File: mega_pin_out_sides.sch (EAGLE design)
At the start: 31 parts, among them T1 2N2222, T2 2N2222, T3 2N2222, T4 2N2222

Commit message: Continue side Schematic design and layout
Almost finished first trail for board layout.
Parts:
- added OK10, OK11, OK12, OK13, OK14, OK15, OK16, OK17, OK18, OK5, OK6, OK7, OK8, OK9: PC817, optocoupler:PC817
- added R10, R11, R12, R13, R14, R15, R16, R17, R18, R19, R20, R21, R22, R23, R24, R25, R26, R27, R28, R29, R30, R31, R32, R33, R34, R35, R36, R9: (no value), resistor:R-US_M1206
- added T10, T11, T12, T13, T14, T15, T16, T17, T18, T5, T6, T7, T8, T9: 2N2222, transistor:2N2222
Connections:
- removed net N$16: X1-5.KL
- new net 0: PWML.1, R23.1
- new net 0BJT: T12.C, X2-2.KL
- new net 14: COMMUNICATION.8, R25.1
- new net 14BJT: T13.C, X2-3.KL
- new net 15: COMMUNICATION.7, R27.1
- new net 15BJT: T14.C, X2-4.KL
- new net 16: COMMUNICATION.6, R29.1
- new net 16BJT: T15.C, X2-5.KL
- new net 17: COMMUNICATION.5, R31.1
- new net 17BJT: T16.C, X2-6.KL
- new net 18: COMMUNICATION.4, R33.1
- new net 18BJT: T17.C, X2-7.KL
- new net 19: COMMUNICATION.3, R35.1
- new net 19BJT: T18.C, X2-8.KL
- new net 2: PWML.3, R21.1
- new net 2BJT: T11.C, X2-1.KL
- new net 3: PWML.4, R19.1
- new net 3BJT: T10.C, X1-10.KL
- new net 4: PWML.5, R17.1
- new net 4BJT: T9.C, X1-9.KL
- new net 5: PWML.6, R15.1
- new net 5BJT: T8.C, X1-8.KL
- new net 6: PWML.7, R13.1
- new net 6BJT: T7.C, X1-7.KL
- new net 7: PWML.8, R11.1
- new net 7BJT: T6.C, X1-6.KL
- new net 8: JP6.10, R9.1
- new net 8BJT: T5.C, X1-5.KL
- new net N$14: OK5.A, R9.2
- new net N$15: OK5.EMIT, R10.1
- new net N$22: R10.2, T5.B
- new net N$23: OK6.A, R11.2
- new net N$24: OK6.EMIT, R12.1
- new net N$25: R12.2, T6.B
- new net N$26: OK7.A, R13.2
- new net N$27: OK7.EMIT, R14.1
- new net N$28: R14.2, T7.B
- new net N$29: OK8.A, R15.2
- new net N$30: OK8.EMIT, R16.1
- new net N$31: R16.2, T8.B
- new net N$32: OK9.A, R17.2
- new net N$33: OK9.EMIT, R18.1
- new net N$34: R18.2, T9.B
- new net N$35: OK10.A, R19.2
- new net N$36: OK10.EMIT, R20.1
- new net N$37: R20.2, T10.B
- new net N$38: OK11.A, R21.2
- new net N$39: OK11.EMIT, R22.1
- new net N$40: R22.2, T11.B
- new net N$41: OK16.A, R31.2
- new net N$42: OK16.EMIT, R32.1
- new net N$43: R32.2, T16.B
- new net N$44: OK12.A, R23.2
- new net N$45: OK12.EMIT, R24.1
- new net N$46: R24.2, T12.B
- new net N$47: OK13.A, R25.2
- new net N$48: OK13.EMIT, R26.1
- new net N$49: R26.2, T13.B
- new net N$50: OK14.A, R27.2
- new net N$51: OK14.EMIT, R28.1
- new net N$52: R28.2, T14.B
- new net N$53: OK15.A, R29.2
- new net N$54: OK15.EMIT, R30.1
- new net N$55: R30.2, T15.B
- new net N$56: OK18.A, R35.2
- new net N$57: OK18.EMIT, R36.1
- new net N$58: R36.2, T18.B
- new net N$59: OK17.A, R33.2
- new net N$60: OK17.EMIT, R34.1
- new net N$61: R34.2, T17.B
- new net N$77: COMMUNICATION.2
- new net N$78: COMMUNICATION.1
- new net N$92: X2-9.KL
- new net N$93: X2-10.KL
- net GND: now also OK10.C, OK11.C, OK12.C, OK13.C, OK14.C, OK15.C, OK16.C, OK17.C, OK18.C, OK5.C, OK6.C, OK7.C, OK8.C, OK9.C, T10.E, T11.E, T12.E, T13.E, T14.E, T15.E, T16.E, T17.E, T18.E, T5.E, T6.E, T7.E, T8.E, T9.E
- net VEXT: now also OK10.COL, OK11.COL, OK12.COL, OK13.COL, OK14.COL, OK15.COL, OK16.COL, OK17.COL, OK18.COL, OK5.COL, OK6.COL, OK7.COL, OK8.COL, OK9.COL
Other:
- moved on the sheet: C1, C2, OK1, OK2, OK3, OK4, R1, R2, R3, R4, R5, R6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

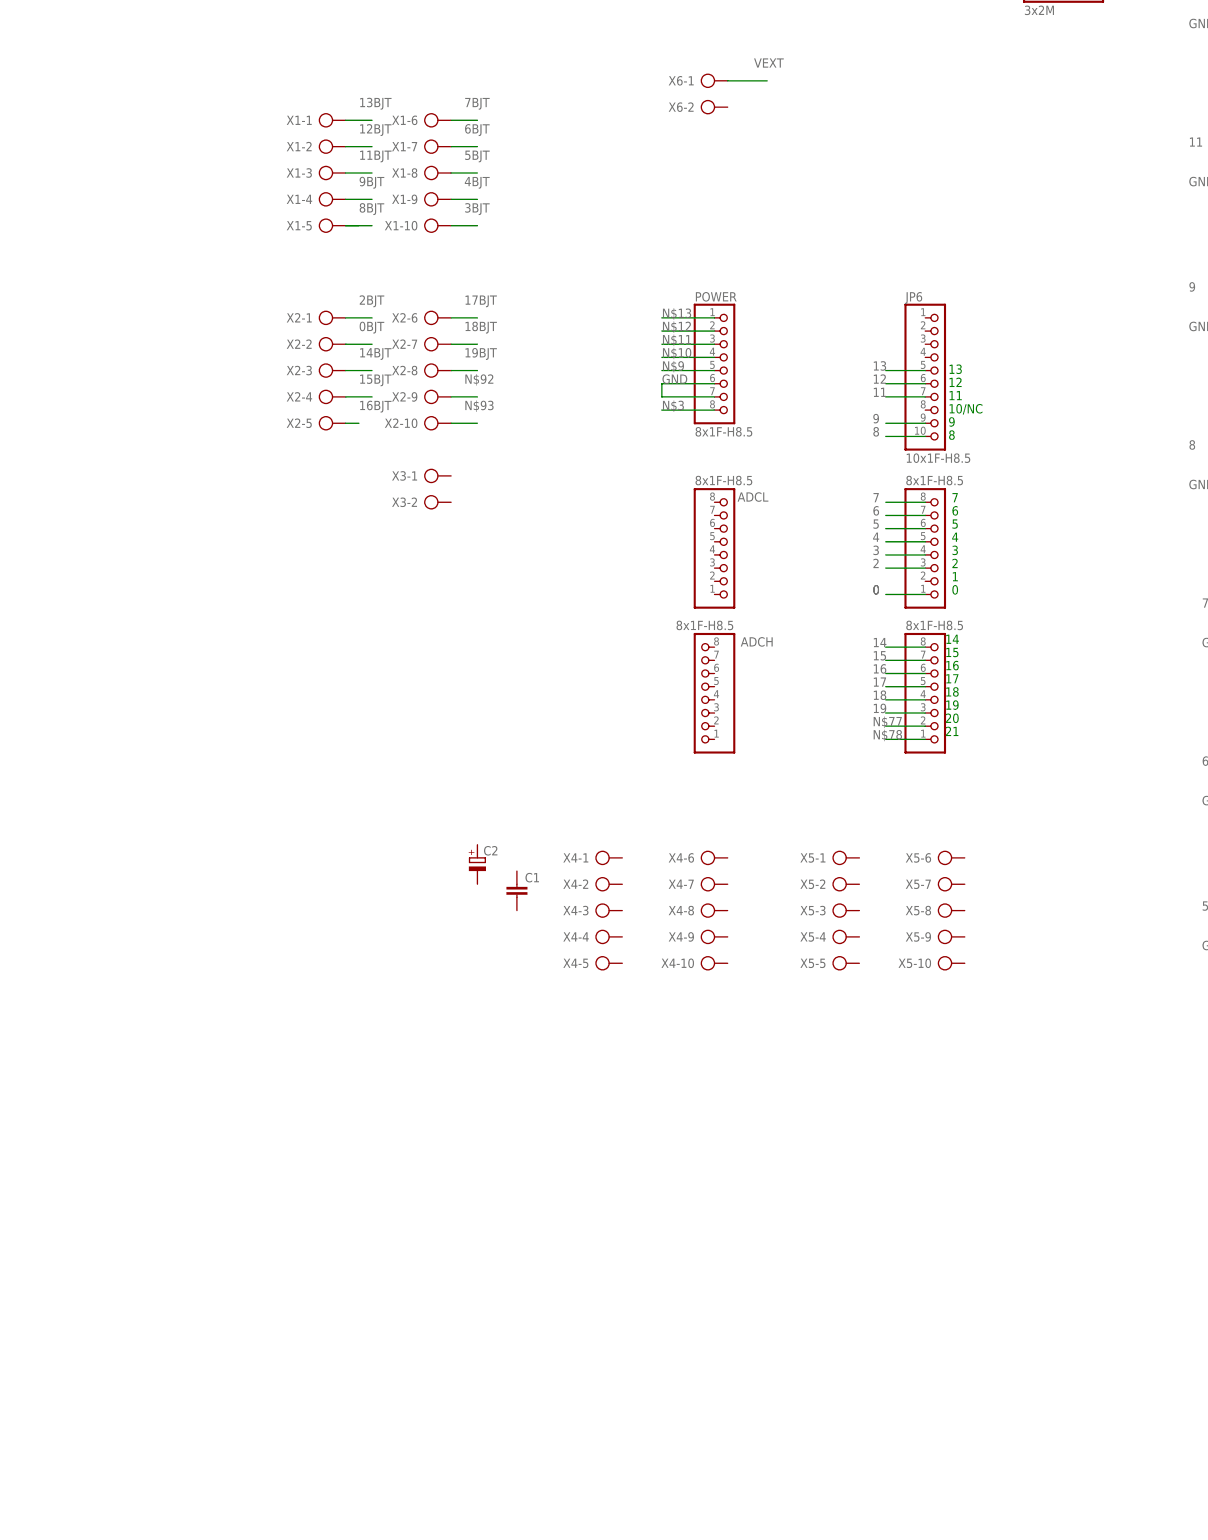
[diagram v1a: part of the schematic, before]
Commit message: [SIDES] New design proposal
- In this commit the layout was completely changed. Opto are grouped in the center while BJT was beside the terminal blocks.

TODO: complete the Analogue side.
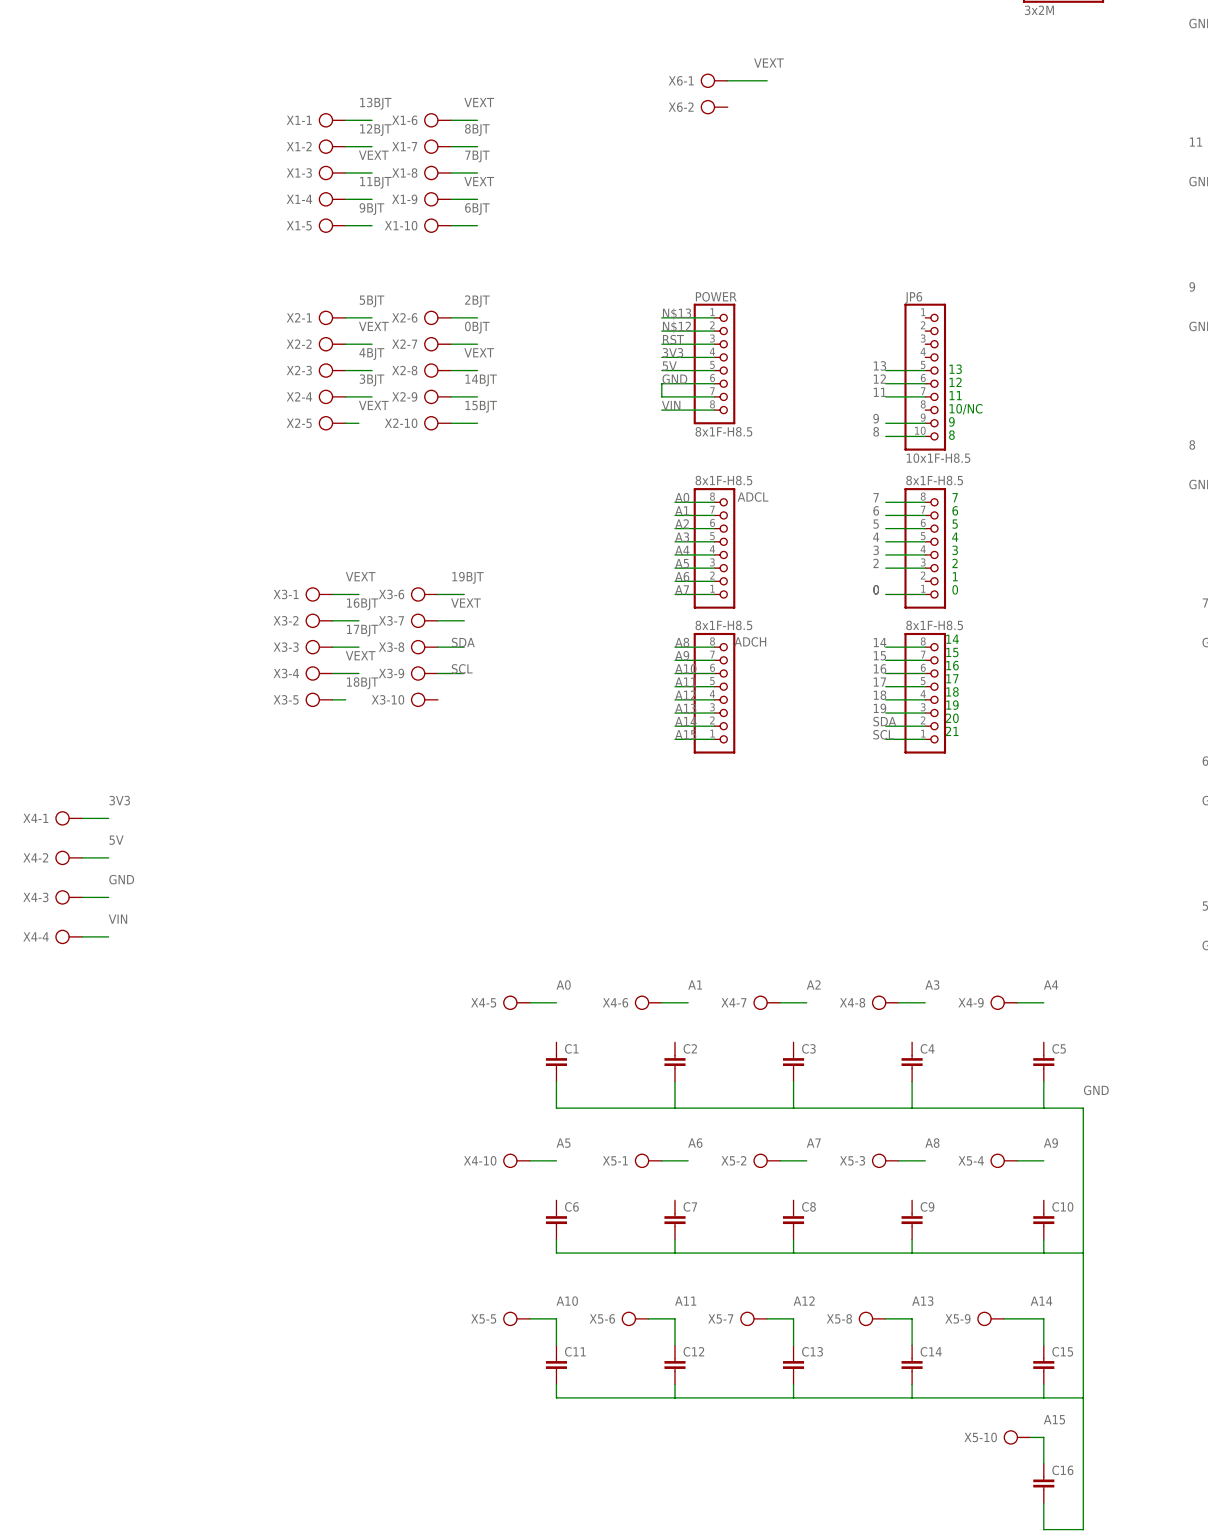
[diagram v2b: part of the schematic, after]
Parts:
- added C10, C11, C12, C13, C14, C15, C16, C3, C4, C5, C6, C7, C8, C9: (no value), resistor:C-EUC1206
- C2: device rcl:CPOL-EUE2.5-6 -> resistor:C-EUC1206
- X3: device con-ptr500:AK500/2 -> con-ptr500:AK500/10
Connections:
- net N$11 renamed RST
- removed net N$10: POWER.4
- removed net N$3: POWER.8
- removed net N$77: COMMUNICATION.2
- removed net N$78: COMMUNICATION.1
- removed net N$9: POWER.5
- removed net N$92: X2-9.KL
- removed net N$93: X2-10.KL
- new net 3V3: POWER.4, X4-1.KL
- new net 5V: POWER.5, X4-2.KL
- new net A0: ADCL.8, X4-5.KL
- new net A1: ADCL.7, X4-6.KL
- new net A10: ADCH.6, C11.1, X5-5.KL
- new net A11: ADCH.5, C12.1, X5-6.KL
- new net A12: ADCH.4, C13.1, X5-7.KL
- new net A13: ADCH.3, C14.1, X5-8.KL
- new net A14: ADCH.2, C15.1, X5-9.KL
- new net A15: ADCH.1, C16.1, X5-10.KL
- new net A2: ADCL.6, X4-7.KL
- new net A3: ADCL.5, X4-8.KL
- new net A4: ADCL.4, X4-9.KL
- new net A5: ADCL.3, X4-10.KL
- new net A6: ADCL.2, X5-1.KL
- new net A7: ADCL.1, X5-2.KL
- new net A8: ADCH.8, X5-3.KL
- new net A9: ADCH.7, X5-4.KL
- new net SCL: COMMUNICATION.1, X3-9.KL
- new net SDA: COMMUNICATION.2, X3-8.KL
- new net VIN: POWER.8, X4-4.KL
- net 0BJT: now also X2-7.KL; no longer X2-2.KL
- net 11BJT: now also X1-4.KL; no longer X1-3.KL
- net 14BJT: now also X2-9.KL; no longer X2-3.KL
- net 15BJT: now also X2-10.KL; no longer X2-4.KL
- net 16BJT: now also X3-2.KL; no longer X2-5.KL
- net 17BJT: now also X3-3.KL; no longer X2-6.KL
- net 18BJT: now also X3-5.KL; no longer X2-7.KL
- net 19BJT: now also X3-6.KL; no longer X2-8.KL
- net 2BJT: now also X2-6.KL; no longer X2-1.KL
- net 3BJT: now also X2-4.KL; no longer X1-10.KL
- net 4BJT: now also X2-3.KL; no longer X1-9.KL
- net 5BJT: now also X2-1.KL; no longer X1-8.KL
- net 6BJT: now also X1-10.KL; no longer X1-7.KL
- net 7BJT: now also X1-8.KL; no longer X1-6.KL
- net 8BJT: now also X1-7.KL; no longer X1-5.KL
- net 9BJT: now also X1-5.KL; no longer X1-4.KL
- net GND: now also C1.2, C10.2, C11.2, C12.2, C13.2, C14.2, C15.2, C16.2, C2.2, C3.2, C4.2, C5.2, C6.2, C7.2, C8.2, C9.2, X4-3.KL
- net VEXT: now also X1-3.KL, X1-6.KL, X1-9.KL, X2-2.KL, X2-5.KL, X2-8.KL, X3-1.KL, X3-4.KL, X3-7.KL
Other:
- moved on the sheet: C1, X3-1, X3-2, X4-1, X4-10, X4-2, X4-3, X4-4, X4-5, X4-6, X4-7, X4-8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

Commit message: [SIDES] Fix major issue where GND was common
- Fix a major bug in the design where the Vext GND and Arduino GND were common. They have been isolated correctly.
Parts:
- C1, C10, C11, C12, C13, C14, C15, C16, C2, C3, C4, C5, C6, C7, C8, C9: device resistor:C-EUC1206 -> adafruit:CPOL-USE2-4
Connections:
- new net GNDEXT: T1.E, T10.E, T11.E, T12.E, T13.E, T14.E, T15.E, T16.E, T17.E, T18.E, T2.E, T3.E, T4.E, T5.E, T6.E, T7.E, T8.E, T9.E, X6-2.KL
- net A0: now also ADCL.1, C1.+; no longer ADCL.8
- net A1: now also ADCL.2, C2.+; no longer ADCL.7
- net A10: now also ADCH.3, C11.+; no longer ADCH.6, C11.1
- net A11: now also ADCH.4, C12.+; no longer ADCH.5, C12.1
- net A12: now also ADCH.5, C13.+; no longer ADCH.4, C13.1
- net A13: now also ADCH.6, C14.+; no longer ADCH.3, C14.1
- net A14: now also ADCH.7, C15.+; no longer ADCH.2, C15.1
- net A15: now also ADCH.8, C16.+; no longer ADCH.1, C16.1
- net A2: now also ADCL.3, C3.+; no longer ADCL.6
- net A3: now also ADCL.4, C4.+; no longer ADCL.5
- net A4: now also ADCL.5, C5.+; no longer ADCL.4
- net A5: now also ADCL.6, C6.+; no longer ADCL.3
- net A6: now also ADCL.7, C7.+; no longer ADCL.2
- net A7: now also ADCL.8, C8.+; no longer ADCL.1
- net A8: now also ADCH.1, C9.+; no longer ADCH.8
- net A9: now also ADCH.2, C10.+; no longer ADCH.7
- net GND: now also C1.-, C10.-, C11.-, C12.-, C13.-, C14.-, C15.-, C16.-, C2.-, C3.-, C4.-, C5.-, C6.-, C7.-, C8.-, C9.-; no longer C1.2, C10.2, C11.2, C12.2, C13.2, C14.2, C15.2, C16.2, C2.2, C3.2, C4.2, C5.2, C6.2, C7.2, C8.2, C9.2, T1.E, T10.E, T11.E, T12.E, T13.E, T14.E, T15.E, T16.E, T17.E, T18.E, T2.E, T3.E, T4.E, T5.E, T6.E, T7.E, T8.E, T9.E

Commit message: [SIDES] Fix DRC Errors
- Fixed all DRC Errors which were related to silk screens mainly.
- Re routed some pins for a better path.
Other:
- moved on the sheet: OK1, OK17, OK18, OK9, R1, R17, R18, R2, R33, R34, R35, R36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
